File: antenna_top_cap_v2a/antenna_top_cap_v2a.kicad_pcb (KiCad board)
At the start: 4 copper layers, 100 x 100 mm, 47 parts, among them J1 DEBUG, J12 USB_C_Receptacle_USB2.0_16P, J2 Battery Charge Bypass, J3 FC Reset Jumper, J4 FC USB Bootselect Jumper, J5 Conn_Coaxial, Q1 BSS138, U1 VL6180XV0NR/1, U16 MCP9808T-E/MS, U2 LP5907-2.8V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

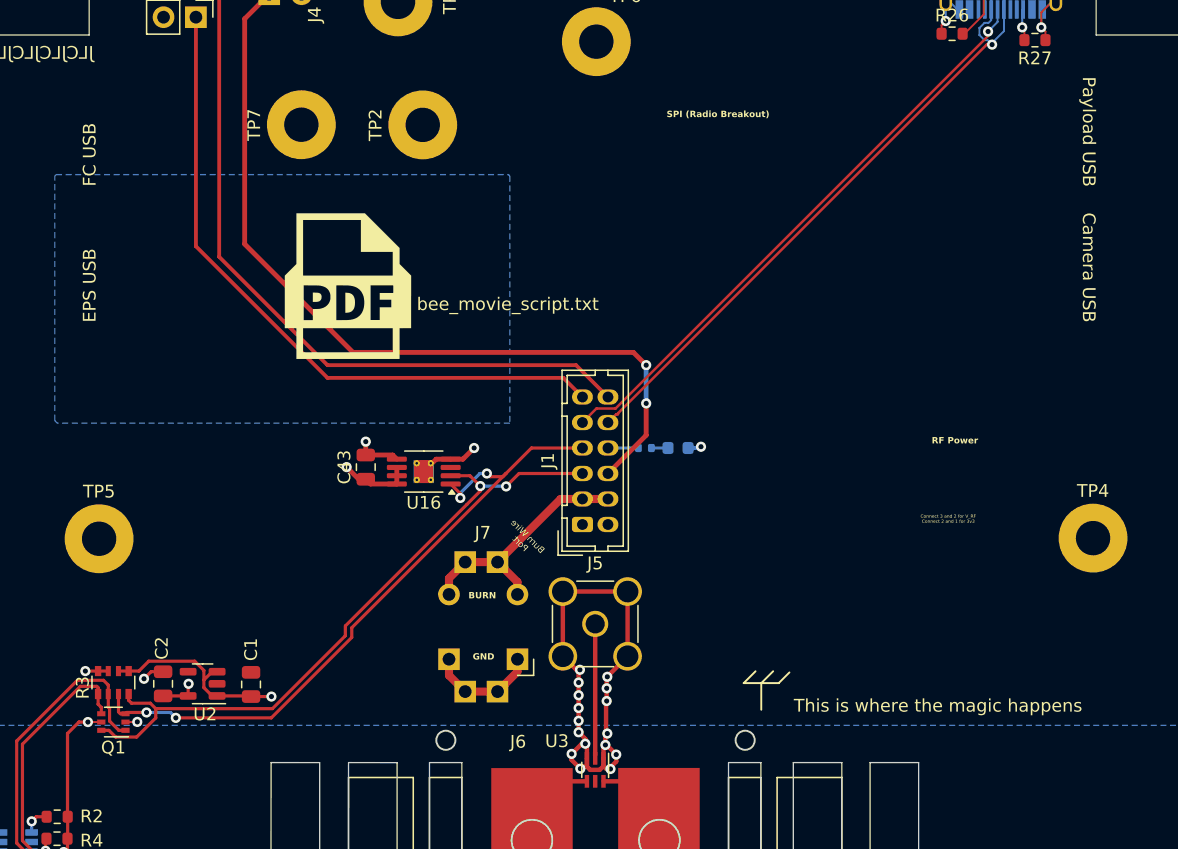
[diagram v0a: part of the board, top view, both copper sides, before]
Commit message: Added VEML7700 Light Sensor
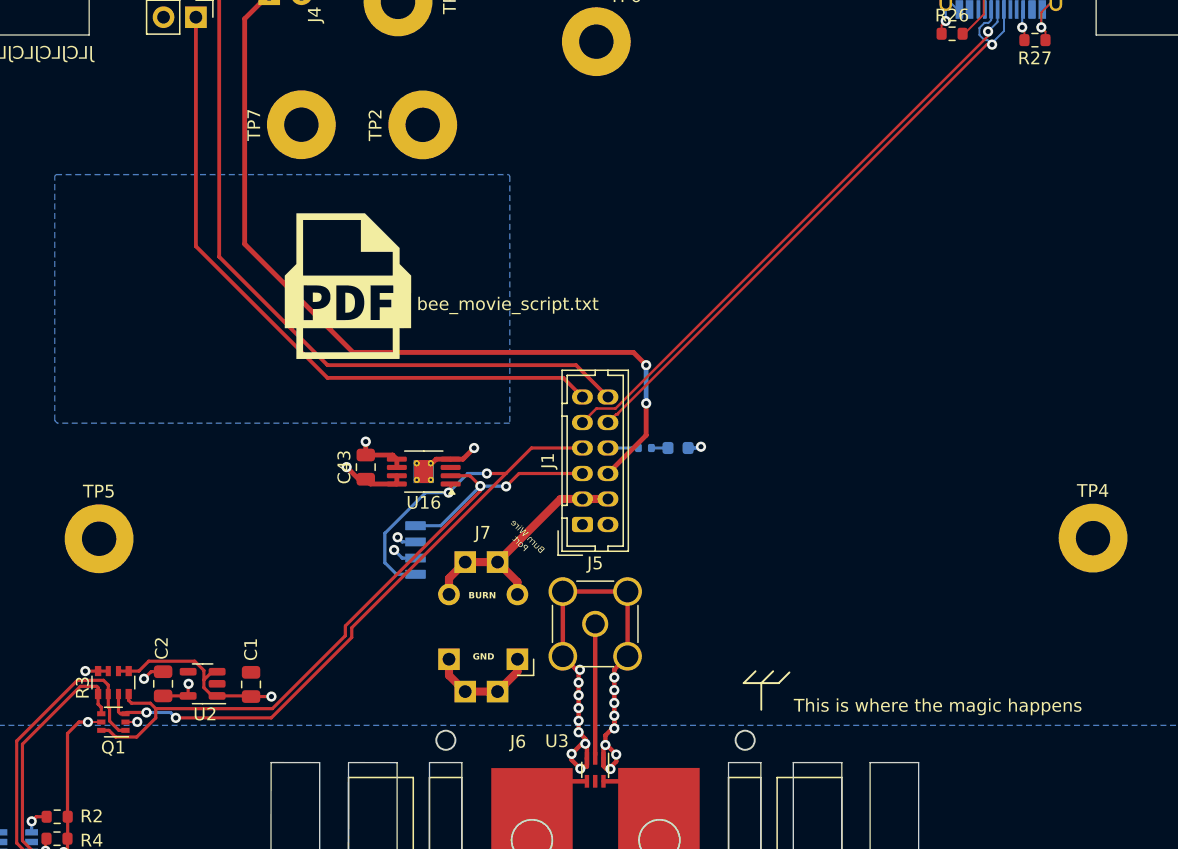
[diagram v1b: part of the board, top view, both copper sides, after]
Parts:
- added U4: VEML7700, VEML7700-TT:XDCR_VEML7700-TT, B.Cu at (150.7, 113.1)
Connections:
- U16 pad 6: +3V3 -> GND
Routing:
- net SDA0: track 53.5 -> 64.6 mm
- net SCL0: track 53.2 -> 59.6 mm
- net GND: track 78.5 -> 79.4 mm, vias 24 -> 26
- net +3V3: track 23.7 -> 24.6 mm, vias 2 -> 3
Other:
- board text removed: "Camera USB"
- board text removed: "Connect 3 and 2 for V_RF Connect 2 and 1 for 3v3"
- board text removed: "EPS USB"
- board text removed: "Payload USB"
- board text removed: "RF Power"
- board text removed: "SPI (Radio Breakout)"

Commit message: Production Files as Ordered 4/17/2025
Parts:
- removed U3: NCS1.5-232+, RF_Converter:Balun_Johanson_0896BM15A0001
- added U5: HHM1591D1, easyeda2kicad:XFMR-SMD_HHM1591D1, F.Cu at (166.0, 131.6)
- moved G*** 2.17 mm to (186.6, 95.0)
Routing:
- net GND: track 79.4 -> 85.4 mm, vias 26 -> 25
- net Net-(J6-tape_1): track 1.66 -> 5.03 mm
- net Net-(J6-tape_2): track 1.40 -> 4.72 mm
- net Net-(J5-In): track 10.3 -> 12.2 mm
- net BURN: track 20.1 -> 18.6 mm
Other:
- board text added: "JLCJLCJLC"
- board text removed: "JLCJLCJLCJLC"
